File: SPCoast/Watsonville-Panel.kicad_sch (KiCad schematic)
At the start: 8 parts, among them U16034 0x2D

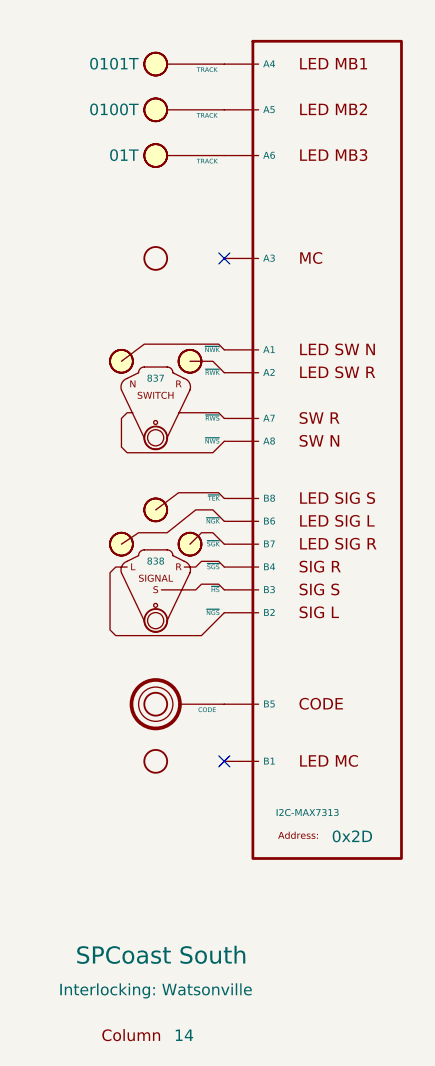
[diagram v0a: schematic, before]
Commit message: chore(kicad): SPCoast symbols refreshed, field attribute visibility, no-connects on unused pins (owner's edit, baseline)
Owner, 2026-10-08: updated symbols from the libraries (the field pin direction flip, InterlockingPlant
61269e0), adjusted attribute visibility, added 22 no-connect markers on unused pins.

Verified (committed as saved, no edits):
- 485 components, 648 nets; every net identical to the previous commit.
- ERC 53 -> 20 messages (13 errors, 7 warnings). Remaining: unconnected HOUSE H / aux MC pins
  (Gilroy Caltrain, Luchessa, Watsonville); Corporal SW11901 still Railroad:Switch_HandThrow (not in
  the library) with open N/R legs; Sargent switch 1 open N/R legs; Christopher Panel U10029 A6 open
  while lamp LMP10093 carries a no-connect; 5 inherited wire stubs.
- Every instance path starts at the root uuid.

Co-Authored-By: Claude Opus 5.5 <noreply@anthropic.com>
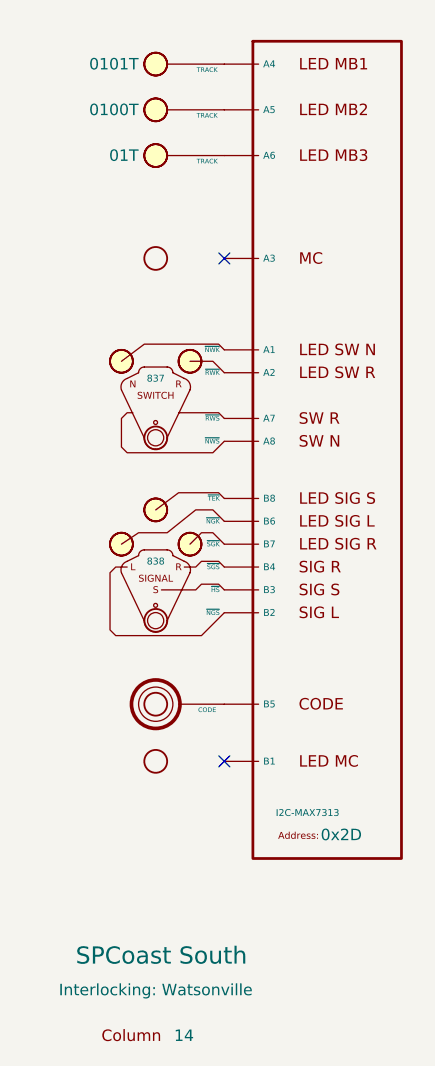
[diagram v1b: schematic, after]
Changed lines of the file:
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@@
+			)
+		)
+		(property "NGS" ""
+			(at 80.01 83.82 0)
+			(hide yes)
+			(show_name no)
+			(do_not_autoplace no)
+			(effects
+				(font
+					(size 1.27 1.27)
+				)
+			)
+		)
+		(property "HS" ""
+			(at 80.01 83.82 0)
+			(hide yes)
+			(show_name no)
+			(do_not_autoplace no)
+			(effects
+				(font
+					(size 1.27 1.27)
+				)
+			)
+		)
+		(property "SGS" ""
+			(at 80.01 83.82 0)
+			(hide yes)
+			(show_name no)
+			(do_not_autoplace no)
+			(effects
+				(font
+					(size 1.27 1.27)
+				)
+			)
+		)
+		(property "SGK" ""
+			(at 80.01 83.82 0)
+			(hide yes)
+			(show_name no)
+			(do_not_autoplace no)
+			(effects
+				(font
+					(size 1.27 1.27)
+				)
+			)
+		)
+		(property "NGK" ""
+			(at 80.01 83.82 0)
+			(hide yes)
+			(show_name no)
+			(do_not_autoplace no)
+			(effects
+				(font
+					(size 1.27 1.27)
+				)
+			)
+		)
+		(property "TEK" ""
+			(at 80.01 83.82 0)
+			(hide yes)
+			(show_name no)
+			(do_not_autoplace no)
+			(effects
+				(font
+					(size 1.27 1.27)
+				)
 			)
 		)
@@
 			)
 		)
+		(property "LAMP" ""
+			(at 80.01 26.67 0)
+			(hide yes)
+			(show_name no)
+			(do_not_autoplace no)
+			(effects
+				(font
+					(size 1.27 1.27)
+				)
+			)
+		)
 		(pin "1"
 		)
@@
 			)
 		)
+		(property "LAMP" ""
+			(at 80.01 36.83 0)
+			(hide yes)
+			(show_name no)
+			(do_not_autoplace no)
+			(effects
+				(font
+					(size 1.27 1.27)
+				)
+			)
+		)
 		(pin "1"
 		)
@@
 			(at 93.345 109.855 0)
 			(show_name no)
-			(do_not_autoplace no)
+			(do_not_autoplace yes)
 			(effects
 				(font
@@
 		)
 		(property "Address" "0x2D"
-			(at 101.854 112.522 0)
+			(at 100.6281 112.3109 0)
 			(show_name no)
 			(do_not_autoplace no)
@@
 			)
 		)
+		(property "CODE" ""
+			(at 80.01 97.79 0)
+			(hide yes)
+			(show_name no)
+			(do_not_autoplace no)
+			(effects
+				(font
+					(size 1.27 1.27)
+				)
+			)
+		)
 		(pin "1"
 		)
@@
 			)
 		)
+		(property "NWS" ""
+			(at 80.01 63.5 0)
+			(hide yes)
+			(show_name no)
+			(do_not_autoplace no)
+			(effects
+				(font
+					(size 1.27 1.27)
+				)
+			)
+		)
+		(property "RWS" ""
+			(at 80.01 63.5 0)
+			(hide yes)
+			(show_name no)
+			(do_not_autoplace no)
+			(effects
+				(font
+					(size 1.27 1.27)
+				)
+			)
+		)
+		(property "RWK" ""
+			(at 80.01 63.5 0)
+			(hide yes)
+			(show_name no)
+			(do_not_autoplace no)
+			(effects
+				(font
+					(size 1.27 1.27)
+				)
+			)
+		)
+		(property "NWK" ""
+			(at 80.01 63.5 0)
+			(hide yes)
+			(show_name no)
+			(do_not_autoplace no)
+			(effects
+				(font
+					(size 1.27 1.27)
+				)
+			)
+		)
 		(pin "1"
 		)
@@
 			(hide yes)
 			(show_name no)
+			(do_not_autoplace no)
+			(effects
+				(font
+					(size 1.27 1.27)
+				)
+			)
+		)
+		(property "LAMP" ""
+			(at 80.01 31.75 0)
+			(hide yes)
+			(show_name no)

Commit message: feat(spcoast): every sheet on the four Railroad libraries (checkpoint step 6, mechanical half)
By SPCoast/edits/2026-10-12-migrate-libraries.py, run once with KiCad closed: 483 instances
remapped across 16 sheets, embedded definitions replaced by the library blocks, instance fields
synced (Kind, ControlToken, Vital, NormalIs, Chain, Index dropped; Indications renamed
IndicationCeiling; Hold_ms renamed hold_ms; a pixel's Index became its Address; Rulebook kept
on the four Luchessa markers because the compiler still reads it), and 22 units added at the
same position for the plates and devices that are multi-unit now. Owner's choices: every plant
head CPL; Sargent's semaphore UQ; the 0x27 PCA9685 as PWM; the office MAX7313s as the
SPCoastcTc variant. Left by hand: the two AUXILIARY_TRAFFIC markers on Watsonville (retired).

Verified (production/migration-gate.txt, netlist_diff.py against pre-migration.net): office
and local plates and all chips keep their connectivity; 14 nets lost, all on Sargent, where
the six field devices (DevSW13001, 13004 to 13007, 13012) have new pin positions and must be
re-wired by hand. ERC: lib_symbol_issues 492 before (unregistered libraries) to 2 after (the
retired markers); the 29 unconnected pins are those devices and their chip pins.

Co-Authored-By: Claude Fable 5.1 <noreply@anthropic.com>
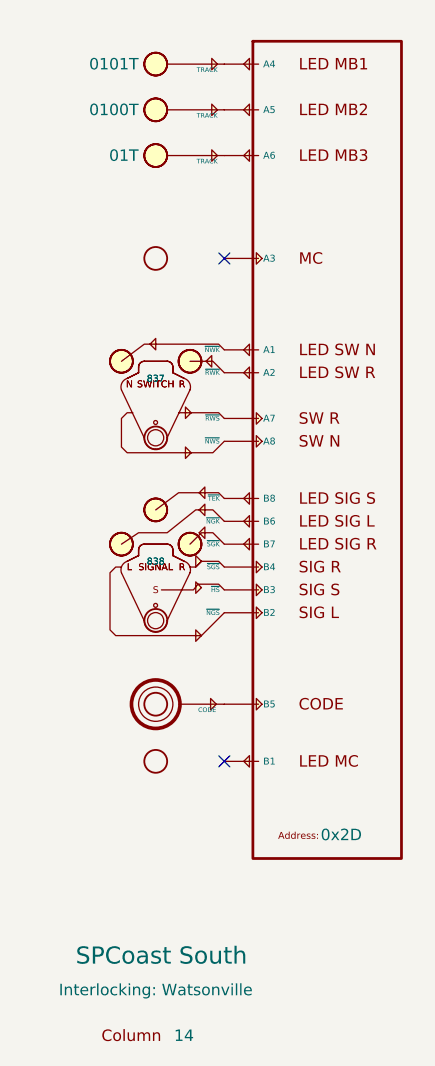
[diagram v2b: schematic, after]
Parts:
- added unit 2 of SGL16014
- added unit 2 of SWL16014
- CDE16014: symbol RailroadPanel:PanelCode -> Railroad-Office:PanelCode; Appliance (none) -> lever; Kind CODE -> (none); Pin.CODE (none) -> binary; Style (none) -> code
- COL16034: symbol RailroadPanel:PanelColumn -> Railroad-Office:PanelColumn
- LMP16141, LMP16142, LMP16143: symbol RailroadPanel:PanelLamp-YELLOW -> Railroad-Office:PanelLamp-YELLOW; Appliance (none) -> lamp; Kind LAMP -> (none); Pin.LAMP (none) -> binary; Style (none) -> indication
- SGL16014: symbol RailroadPanel:PanelSignal -> Railroad-Office:PanelSignal; Appliance (none) -> lever; Kind SIGNAL_LEVER -> (none); Pin.HS (none) -> binary; Pin.NGK (none) -> binary; Pin.NGS (none) -> binary; Pin.SGK (none) -> binary; Pin.SGS (none) -> binary; Pin.TEK (none) -> binary; Style (none) -> signal
- SWL16014: symbol RailroadPanel:PanelSwitch -> Railroad-Office:PanelSwitch; Appliance (none) -> lever; Kind SWITCH_LEVER -> (none); Pin.NWK (none) -> binary; Pin.NWS (none) -> binary; Pin.RWK (none) -> binary; Pin.RWS (none) -> binary; Style (none) -> switch
- U16034: symbol RailroadPanel:Driver-I2C-MAX7313 -> Railroad-HardwareIO:Driver-I2C-MAX7313-SPCoastcTc; IC (none) -> MAX7313; Kind I2C-MAX7313 -> (none); Pin.A1 (none) -> binary; Pin.A2 (none) -> binary; Pin.A3 (none) -> binary; Pin.A4 (none) -> binary; Pin.A5 (none) -> binary; Pin.A6 (none) -> binary; Pin.A7 (none) -> binary; Pin.A8 (none) -> binary; Pin.B1 (none) -> binary; Pin.B2 (none) -> binary; Pin.B3 (none) -> binary; Pin.B4 (none) -> binary; Pin.B5 (none) -> binary; Pin.B6 (none) -> binary; Pin.B7 (none) -> binary; Pin.B8 (none) -> binary
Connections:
- net at U16034.15 (B7): now also SGL16014.5 (~{SGK}); no longer SGL16014.5 (~{SGK})
- net at U16034.14 (B6): now also SGL16014.6 (~{NGK}); no longer SGL16014.6 (~{NGK})
- net at U16034.16 (B8): now also SGL16014.7 (~{TEK}); no longer SGL16014.7 (~{TEK})
- net at U16034.1 (A1): now also SWL16014.5 (~{NWK}); no longer SWL16014.5 (~{NWK})
- net at U16034.2 (A2): now also SWL16014.4 (~{RWK}); no longer SWL16014.4 (~{RWK})

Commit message: chore: owner's Sargent cleanup and library edits of 2026-10-12 and 13 (baseline)
Co-Authored-By: Claude Fable 5.1 <noreply@anthropic.com>
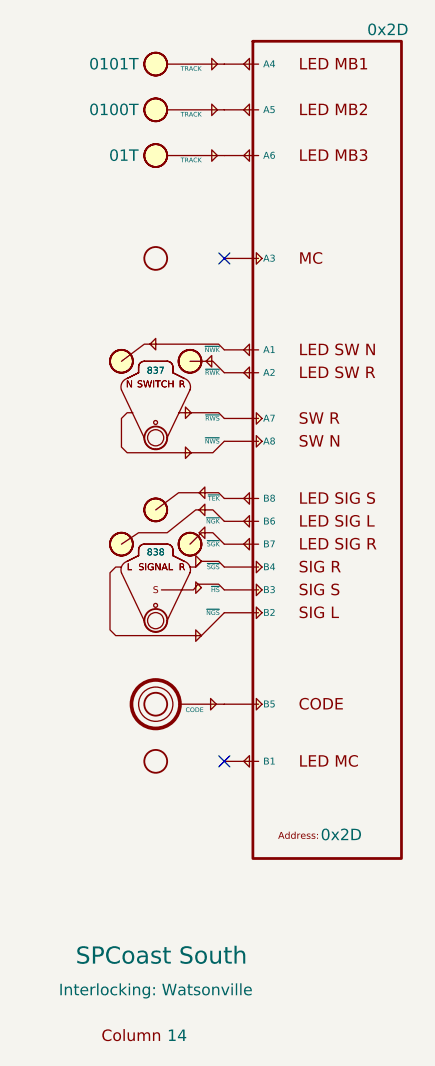
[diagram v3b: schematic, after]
